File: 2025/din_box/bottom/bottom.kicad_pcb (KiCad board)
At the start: 2 copper layers, 32.2 x 83 mm, 37 parts, among them J1 PWR, J2 RS485_Modbus_BAC, J3 Conn_02x02_Odd_Even, J4 RLY, J5 PROG, K1 G6K-2, Q1 2N7002, U1 CH32V003JxMx, U2 SSP3085, U3 ME6209A50M3G

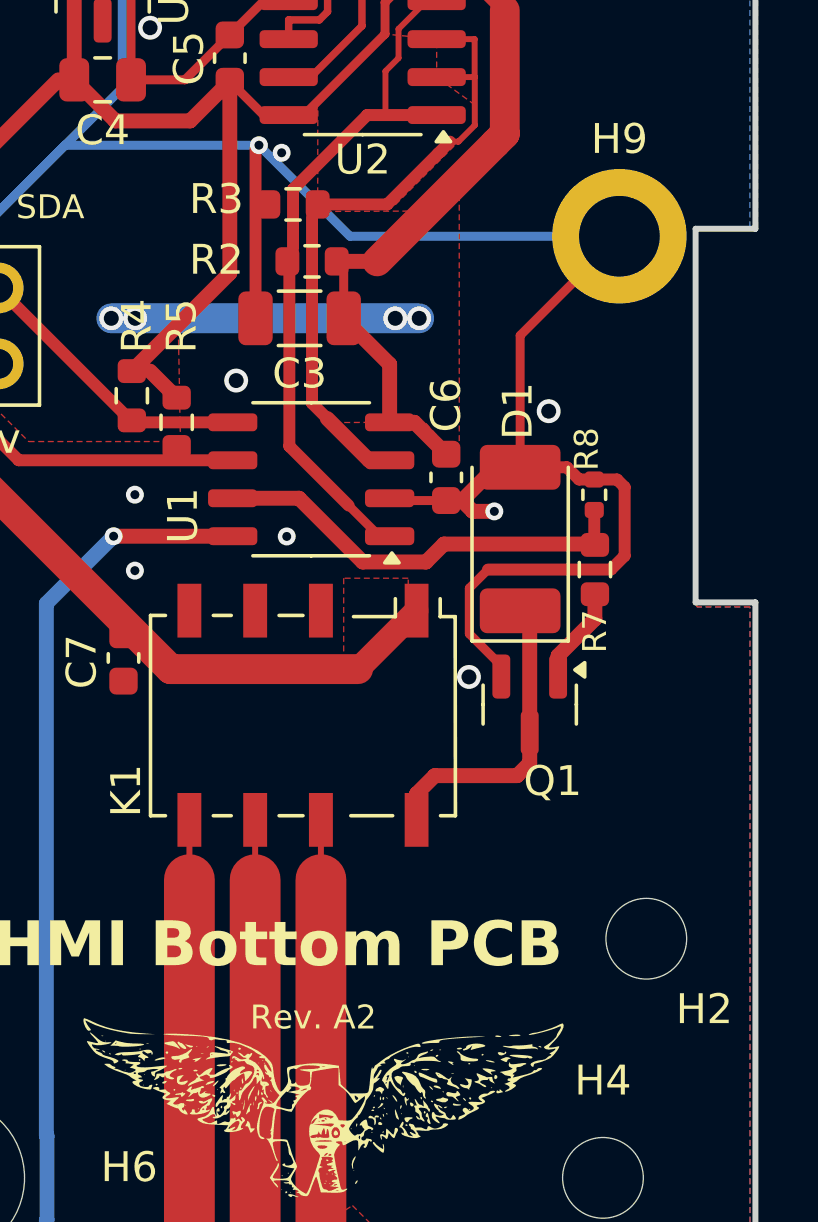
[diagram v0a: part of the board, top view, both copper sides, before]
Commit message: Adding USB-C to RS485 converter board
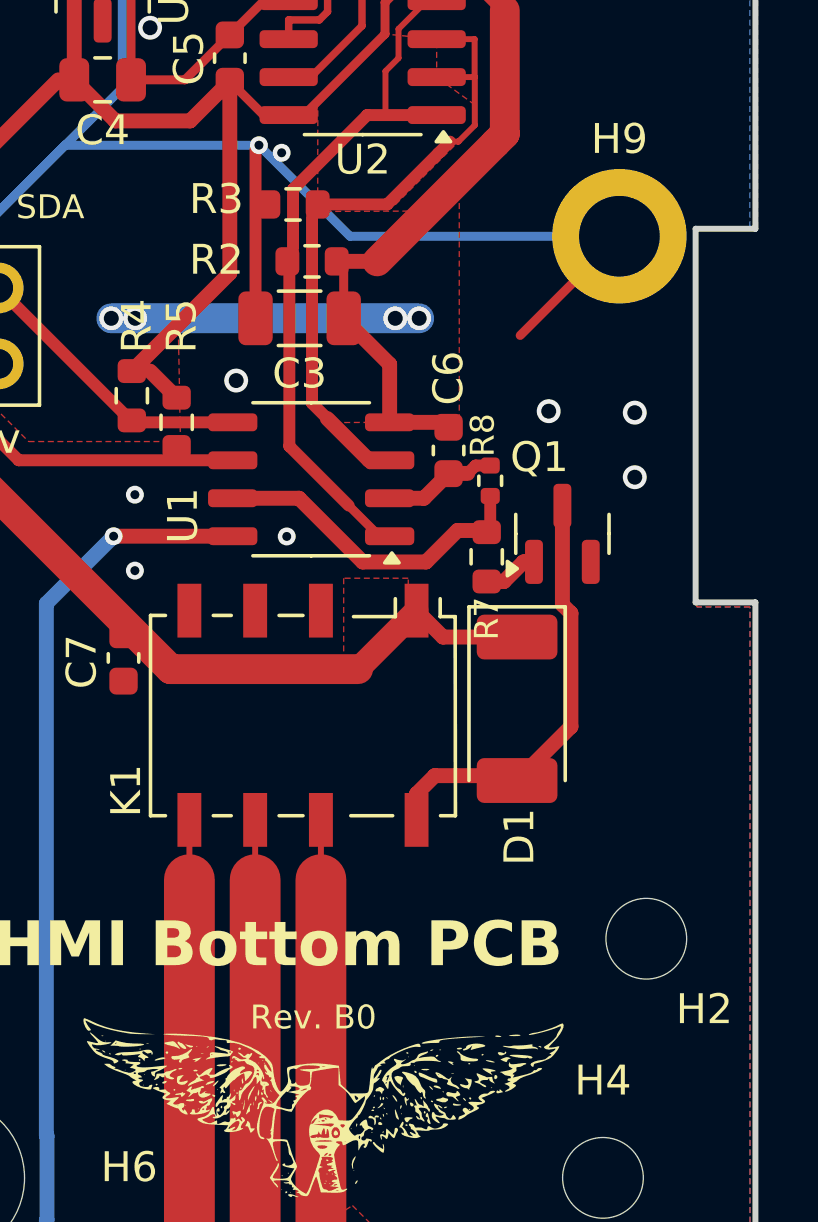
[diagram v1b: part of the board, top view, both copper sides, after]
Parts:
- moved Q1 5.81 mm to (117.5, 109.5), turned to 90 degrees
- moved D1 5.68 mm to (116.0, 115.3), turned to -90 degrees
- moved R7 3.64 mm to (115.0, 110.2)
- moved R8 3.51 mm to (115.1, 107.7)
- moved C6 0.90 mm to (113.7, 106.7)
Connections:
- D1 pad 1: Net-(D1-K) -> +12V
- D1 pad 2: GND -> Net-(D1-A)
- K1 pad 8: Net-(D1-K) -> Net-(D1-A)
- Q1 pad 3: Net-(D1-K) -> Net-(D1-A)
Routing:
- net GND: track 144.2 -> 122.6 mm
- net Net-(D1-A): track 0.00 -> 14.5 mm
- net Net-(D1-K): track 10.3 -> 0.00 mm
- net +12V: track 78.1 -> 81.8 mm
- net /OUT: track 14.4 -> 11.1 mm
- net Net-(Q1-G): track 2.86 -> 1.85 mm
